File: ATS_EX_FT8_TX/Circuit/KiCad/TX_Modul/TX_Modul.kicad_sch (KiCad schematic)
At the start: 11 parts, among them J1 Conn_01x15_Socket, J2 Conn_01x15_Socket, J3 From PC, J4 Relais

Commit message: Update
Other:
- note added: "Nano"
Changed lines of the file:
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@@
+		)
+	)
+	(text "Nano\n"
+		(exclude_from_sim no)
+		(at 127.254 45.974 0)
+		(effects
+			(font
+				(size 1.27 1.27)
+			)
 		)
 	)

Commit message: Update
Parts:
- added J5: Conn_01x02_Socket, symbol Connector:Conn_01x02_Socket
- added J6, J7, J8: Conn_01x06_Socket, symbol Connector:Conn_01x06_Socket
- added Si5351: Conn_01x07_Socket, symbol Connector:Conn_01x07_Socket
- C1, C2, C3: footprint (none) -> Capacitor_THT:C_Disc_D4.7mm_W2.5mm_P5.00mm
- R1, R2, R3, R4: footprint (none) -> Resistor_THT:R_Axial_DIN0204_L3.6mm_D1.6mm_P5.08mm_Horizontal
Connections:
- net at J1.15 (Pin_15), J4.1 (Pin_1): now also J5.2 (Pin_2), J7.4 (Pin_4), Si5351.7 (Pin_7)
- net at J1.14 (Pin_14): now also J5.1 (Pin_1), J7.3 (Pin_3), Si5351.6 (Pin_6)
- net at J1.8 (Pin_8): now also Si5351.5 (Pin_5)
- net at J1.9 (Pin_9): now also Si5351.4 (Pin_4)
- net at J2.1 (Pin_1): now also J7.1 (Pin_1)
- net at J2.2 (Pin_2): now also J7.2 (Pin_2)
- new net: J6.1 (Pin_1), J8.1 (Pin_1)
- new net: J6.2 (Pin_2), J8.2 (Pin_2)
- new net: J6.3 (Pin_3), J8.3 (Pin_3)
- new net: J6.4 (Pin_4), J8.4 (Pin_4)
- new net: J6.5 (Pin_5), J8.5 (Pin_5)
- new net: J6.6 (Pin_6), J8.6 (Pin_6)
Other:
- note added: "3.3V"
- note added: "5V"
- note added: "FT8 In / D7"
- note added: "GND"
- note added: "GND / D6"
- note added: "Levelshifter"
- note added: "RX"
- note added: "Relais / D4"
- note added: "SCL"
- note added: "SCL / A5"
- note added: "SDA"
- note added: "SDA / A4"
- note added: "TX"
- moved on the sheet: C1, C2, C3, J1, J2, J3, J4, R1, R2, R3, R4

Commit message: Update
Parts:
- J1, J2: footprint (none) -> Connector_PinSocket_2.54mm:PinSocket_1x15_P2.54mm_Vertical
- J3, J4: footprint (none) -> Connector_PinHeader_2.54mm:PinHeader_1x03_P2.54mm_Vertical
- J5: footprint (none) -> Connector_PinSocket_2.54mm:PinSocket_1x02_P2.54mm_Vertical
- J6, J7, J8: footprint (none) -> Connector_PinSocket_2.54mm:PinSocket_1x06_P2.54mm_Vertical
- R1, R2, R3, R4: footprint Resistor_THT:R_Axial_DIN0204_L3.6mm_D1.6mm_P5.08mm_Horizontal -> Resistor_THT:R_Axial_DIN0204_L3.6mm_D1.6mm_P7.62mm_Horizontal
- Si5351: footprint (none) -> Connector_PinSocket_2.54mm:PinSocket_1x07_P2.54mm_Vertical
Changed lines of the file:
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@@
 			)
 		)
-		(property "Footprint" ""
+		(property "Footprint" "Connector_PinHeader_2.54mm:PinHeader_1x03_P2.54mm_Vertical"
 			(at 207.01 113.03 0)
 			(effects
@@
 			)
 		)
-		(property "Footprint" ""
+		(property "Footprint" "Connector_PinSocket_2.54mm:PinSocket_1x15_P2.54mm_Vertical"
 			(at 137.16 55.88 0)
 			(effects
@@
 			)
 		)
-		(property "Footprint" "Resistor_THT:R_Axial_DIN0204_L3.6mm_D1.6mm_P5.08mm_Horizontal"
+		(property "Footprint" "Resistor_THT:R_Axial_DIN0204_L3.6mm_D1.6mm_P7.62mm_Horizontal"
 			(at 147.32 113.03 0)
 			(effects
@@
 			)
 		)
-		(property "Footprint" ""
+		(property "Footprint" "Connector_PinSocket_2.54mm:PinSocket_1x06_P2.54mm_Vertical"
 			(at 20.32 46.99 0)
 			(effects
@@
 			)
 		)
-		(property "Footprint" ""
+		(property "Footprint" "Connector_PinSocket_2.54mm:PinSocket_1x06_P2.54mm_Vertical"
 			(at 45.72 46.99 0)
 			(effects
@@
 			)
 		)
-		(property "Footprint" "Resistor_THT:R_Axial_DIN0204_L3.6mm_D1.6mm_P5.08mm_Horizontal"
+		(property "Footprint" "Resistor_THT:R_Axial_DIN0204_L3.6mm_D1.6mm_P7.62mm_Horizontal"
 			(at 125.73 113.03 0)
 			(effects
@@
 			)
 		)
-		(property "Footprint" "Resistor_THT:R_Axial_DIN0204_L3.6mm_D1.6mm_P5.08mm_Horizontal"
+		(property "Footprint" "Resistor_THT:R_Axial_DIN0204_L3.6mm_D1.6mm_P7.62mm_Horizontal"
 			(at 106.68 125.73 0)
 			(effects
@@
 			)
 		)
-		(property "Footprint" ""
+		(property "Footprint" "Connector_PinSocket_2.54mm:PinSocket_1x02_P2.54mm_Vertical"
 			(at 41.91 71.12 0)
 			(effects
@@
 			)
 		)
-		(property "Footprint" ""
+		(property "Footprint" "Connector_PinHeader_2.54mm:PinHeader_1x03_P2.54mm_Vertical"
 			(at 207.01 95.25 0)
 			(effects
@@
 			)
 		)
-		(property "Footprint" ""
+		(property "Footprint" "Connector_PinSocket_2.54mm:PinSocket_1x07_P2.54mm_Vertical"
 			(at 73.66 45.72 0)
 			(effects
@@
 			)
 		)
-		(property "Footprint" "Resistor_THT:R_Axial_DIN0204_L3.6mm_D1.6mm_P5.08mm_Horizontal"
+		(property "Footprint" "Resistor_THT:R_Axial_DIN0204_L3.6mm_D1.6mm_P7.62mm_Horizontal"
 			(at 106.68 100.33 0)
 			(effects
@@
 			)
 		)
-		(property "Footprint" ""
+		(property "Footprint" "Connector_PinSocket_2.54mm:PinSocket_1x15_P2.54mm_Vertical"
 			(at 149.86 55.88 0)
 			(effects
@@
 			)
 		)
-		(property "Footprint" ""
+		(property "Footprint" "Connector_PinSocket_2.54mm:PinSocket_1x06_P2.54mm_Vertical"
 			(at 38.1 46.99 0)
 			(effects

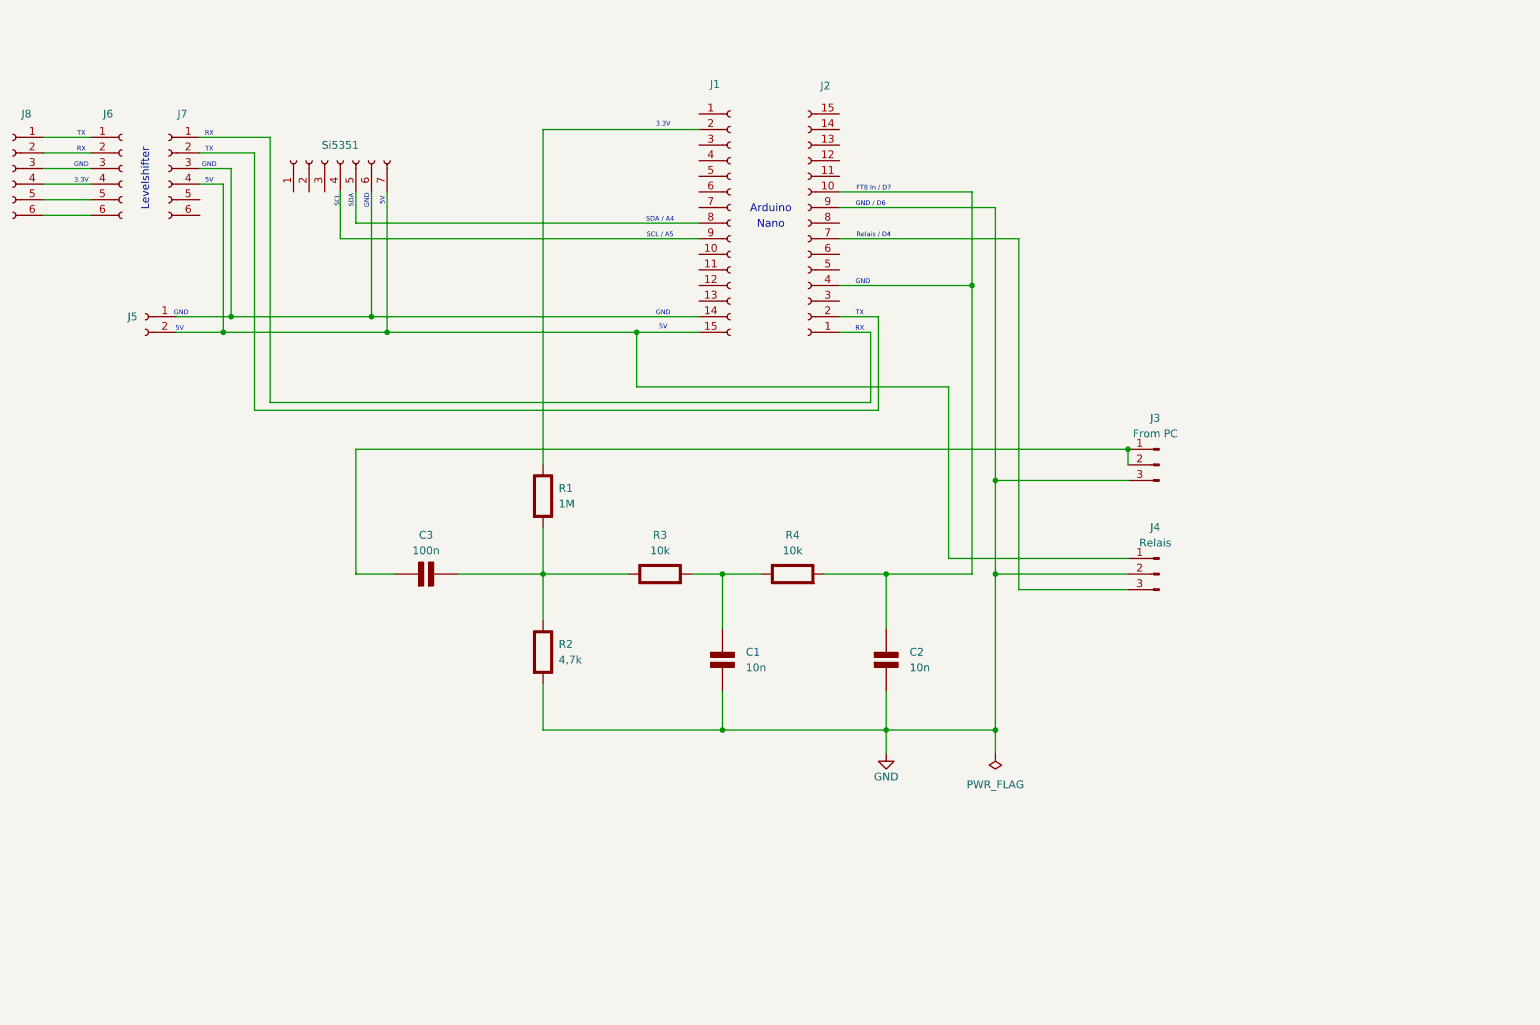
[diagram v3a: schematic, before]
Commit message: update KiCad TX Module
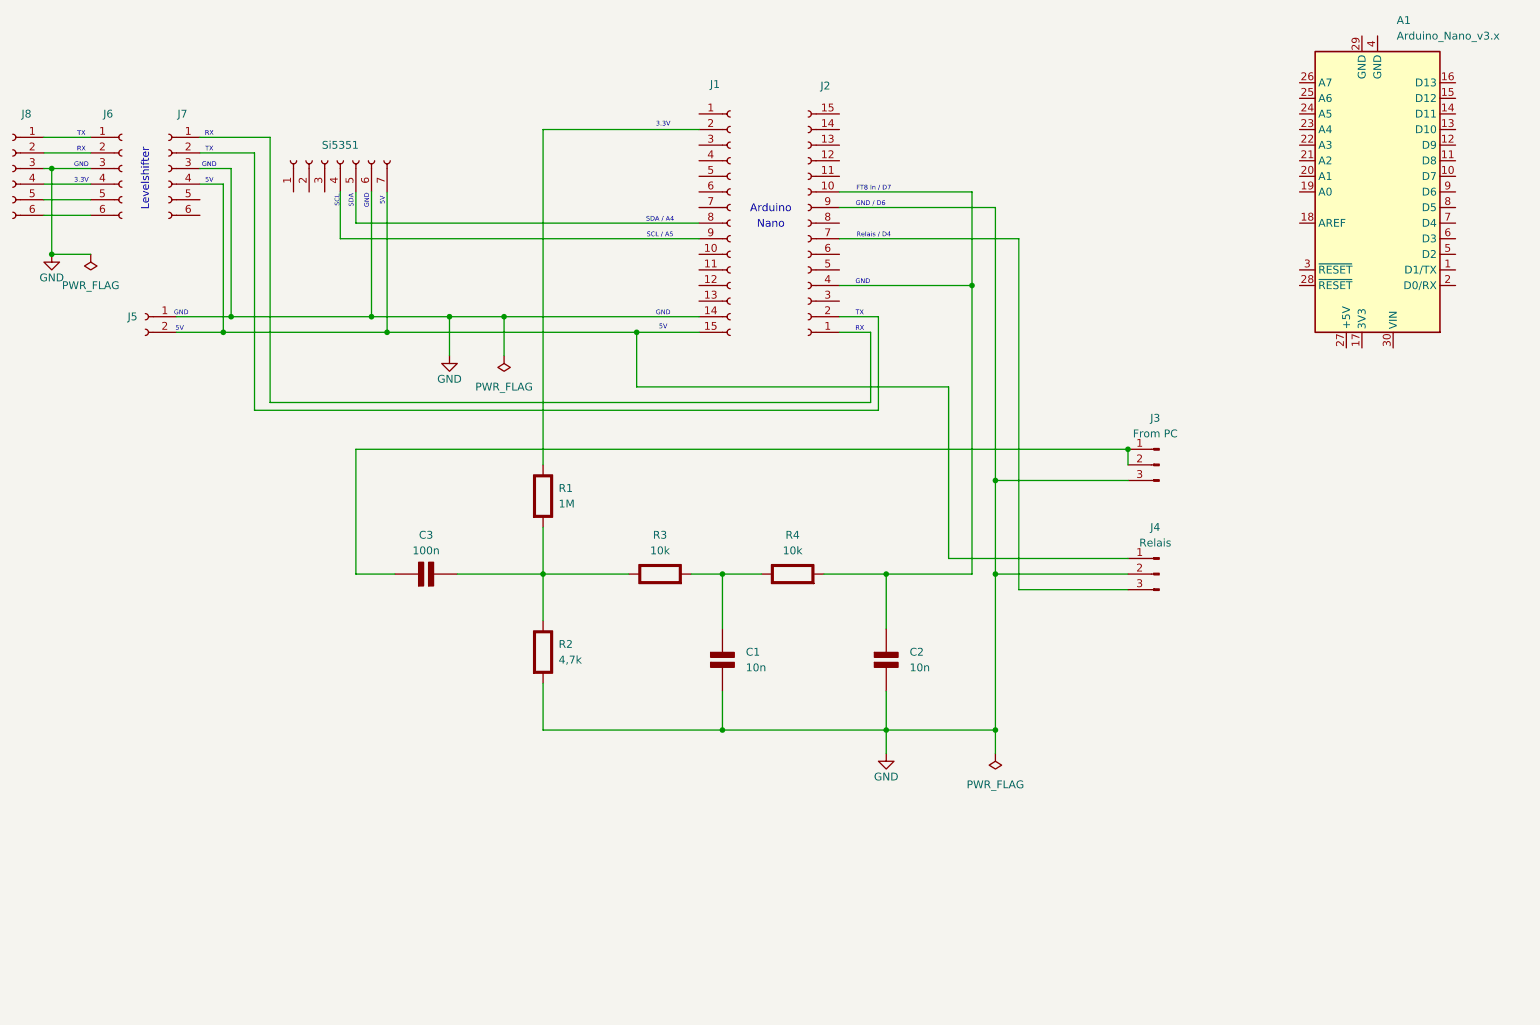
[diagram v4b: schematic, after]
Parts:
- added A1: Arduino_Nano_v3.x, Module:Arduino_Nano, symbol MCU_Module:Arduino_Nano_v3.x
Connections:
- net GND: now also J1.14 (Pin_14), J5.1 (Pin_1), J6.3 (Pin_3), J7.3 (Pin_3), J8.3 (Pin_3), Si5351.6 (Pin_6)

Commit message: Update Platine
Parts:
- added Si1: Conn_01x07_Socket, Connector_PinSocket_2.54mm:PinSocket_1x07_P2.54mm_Vertical, symbol Connector:Conn_01x07_Socket
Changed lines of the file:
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@@
+	)
+	(symbol
+		(lib_id "Connector:Conn_01x07_Socket")
+		(at 73.66 36.83 90)
+		(unit 1)
+		(exclude_from_sim no)
+		(in_bom yes)
+		(on_board yes)
+		(dnp no)
+		(property "Reference" "Si1"
+			(at 73.66 34.29 90)
+			(effects
+				(font
+					(size 1.27 1.27)
+				)
+			)
+		)
+		(property "Value" "Conn_01x07_Socket"
+			(at 73.66 34.29 90)
+			(effects
+				(font
+					(size 1.27 1.27)
+				)
+				(hide yes)
+			)
+		)
+		(property "Footprint" "Connector_PinSocket_2.54mm:PinSocket_1x07_P2.54mm_Vertical"
+			(at 73.66 36.83 0)
+			(effects
+				(font
+					(size 1.27 1.27)
+				)
+				(hide yes)
+			)
+		)
+		(property "Datasheet" "~"
+			(at 73.66 36.83 0)
+			(effects
+				(font
+					(size 1.27 1.27)
+				)
+				(hide yes)
+			)
+		)
+		(property "Description" "Generic connector, single row, 01x07, script generated"
+			(at 73.66 36.83 0)
+			(effects
+				(font
+					(size 1.27 1.27)
+				)
+				(hide yes)
+			)
+		)
+		(pin "4"
+		)
+		(pin "3"
+		)
+		(pin "7"
+		)
+		(pin "1"
+		)
+		(pin "2"
+		)
+		(pin "5"
+		)
+		(pin "6"
+		)
+		(instances
+			(project "TX_Modul"
+				(path "/a9cb15dd-917f-4e9c-8fab-e72d6e2fbc01"
+					(reference "Si1")
+					(unit 1)
+				)
+			)
+		)
 	)
 	(symbol

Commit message: Update TX PCB
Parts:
- added H1, H2, H3, H4: MountingHole_M3, MountingHole:MountingHole_3.2mm_M3, symbol PCM_SL_Mechanical:MountingHole_M3

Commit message: Update Schematic
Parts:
- renumbered J5 to 5V1
